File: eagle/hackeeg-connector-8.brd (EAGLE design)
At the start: 116.3 x 34.1 mm, 13 parts

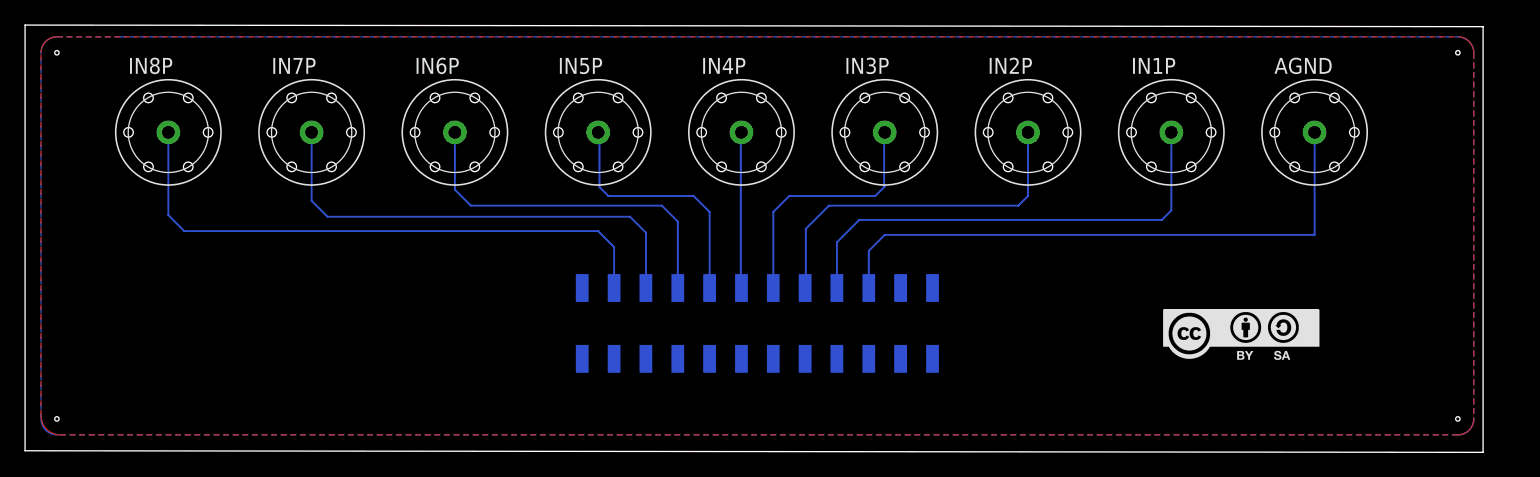
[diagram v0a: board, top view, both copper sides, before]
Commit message: made board smaller; trace width increased to 12mil
- from 8mil
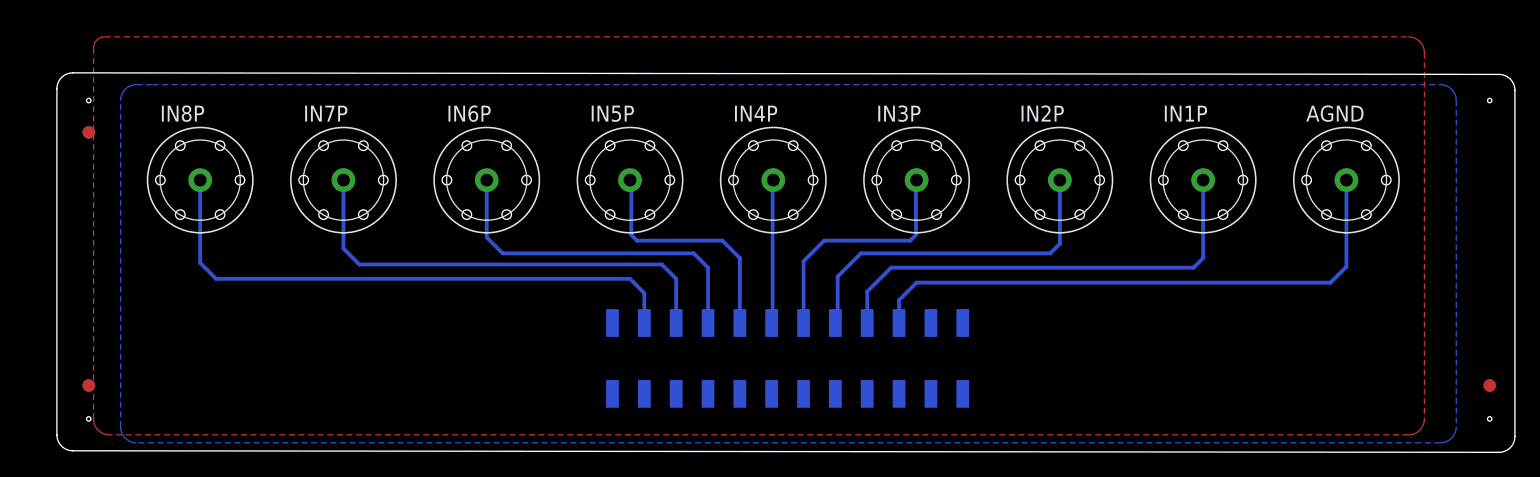
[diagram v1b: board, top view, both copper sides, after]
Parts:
- added FD1, FD2, FD3, FD4, FD5, FD6: FIDUCIAL1X2, SparkFun-Aesthetics:FIDUCIAL-1X2
- moved FRAME1 49.8 mm to (21.6, -10.2), flipped to the top
- moved U$13 14.5 mm to (102.6, 7.11), flipped to the bottom
- moved AGND 4.58 mm to (102.9, 21.6)
- moved IN2P 4.58 mm to (80.0, 21.6)
- moved IN4P 4.58 mm to (57.1, 21.6)
- moved IN5P 4.58 mm to (45.7, 21.6)
- moved IN6P 4.58 mm to (34.3, 21.6)
- moved IN7P 4.58 mm to (22.9, 21.6)
- moved IN8P 4.58 mm to (11.4, 21.6)
- moved U$1 4.58 mm to (22.9, 7.24)
- moved IN1P 4.58 mm to (91.4, 21.6)
- moved IN3P 4.58 mm to (68.6, 21.6)
- moved ELECTRODE-CONNECTOR 3.69 mm to (58.3, 7.37)
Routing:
- net N$1: track 47.2 -> 45.5 mm
- net N$9: track 46.5 -> 45.4 mm
- net N$6: track 20.1 -> 19.0 mm
- net N$8: track 37.6 -> 36.5 mm
- net N$7: track 28.7 -> 27.6 mm
- net N$5: track 12.4 -> 11.4 mm
- net N$3: track 28.6 -> 27.6 mm
- net N$4: track 20.1 -> 19.2 mm
- net N$2: track 37.6 -> 36.6 mm
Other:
- board size 116.3 x 34.1 mm -> 116.3 x 30.3 mm

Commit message: updated libraries, rerouted board
- used new SnapEDA footprint for electrode connector
- updated po-37729 to hex110 package
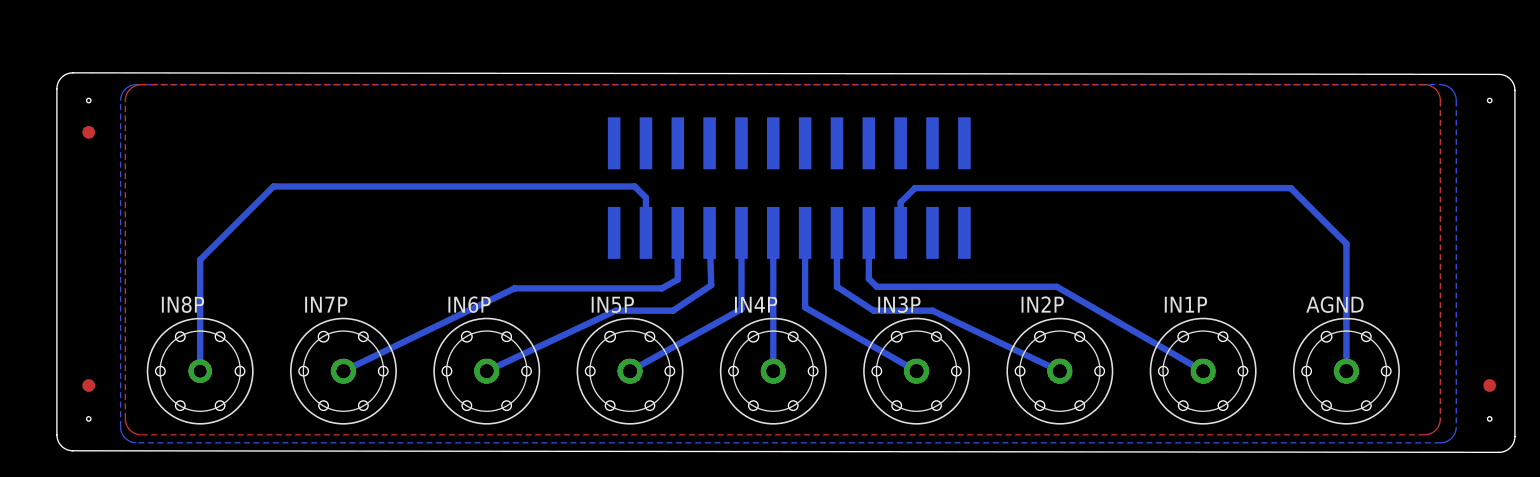
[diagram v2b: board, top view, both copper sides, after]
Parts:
- AGND, IN1P, IN2P, IN3P, IN4P, IN5P, IN6P, IN7P: value PO37729HEX-100 -> PO37729HEX-110; device po-37729:HEX-100 -> po-37729:HEX-110
- ELECTRODE-CONNECTOR: value SBH11-NBPC-D12-SM-BKJ -> SBH11-NBPC-D12-SM-BK; device SBH11-NBPC-D12-SM-BK:SBH11-NBPC-D12-SM-BK -> SBH11-NBPC-D12-SM-BK:SULLINS_SBH11-NBPC-D12-SM-BK
- moved U$13 15.5 mm to (105.2, 22.4)
- moved AGND 15.2 mm to (102.9, 6.35)
- moved IN1P 15.2 mm to (91.4, 6.35)
- moved IN2P 15.2 mm to (80.0, 6.35)
- moved IN3P 15.2 mm to (68.6, 6.35)
- moved IN4P 15.2 mm to (57.1, 6.35)
- moved IN5P 15.2 mm to (45.7, 6.35)
- moved IN6P 15.2 mm to (34.3, 6.35)
- moved IN7P 15.2 mm to (22.9, 6.35)
- moved IN8P 15.2 mm to (11.4, 6.35)
- moved U$1 14.5 mm to (19.1, 21.2)
- moved ELECTRODE-CONNECTOR 13.6 mm to (58.4, 21.0)
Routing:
- net N$1: track 45.5 -> 50.5 mm
- net N$9: track 45.4 -> 50.1 mm
- net N$8: track 36.5 -> 32.1 mm
- net N$2: track 36.6 -> 32.4 mm
- net N$3: track 27.6 -> 23.7 mm
- net N$7: track 27.6 -> 23.8 mm
- net N$4: track 19.2 -> 16.2 mm
- net N$6: track 19.0 -> 16.3 mm
